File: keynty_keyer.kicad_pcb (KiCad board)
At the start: 2 copper layers, 60 x 35 mm, 32 parts, among them J1 Key Input, J2 Conn_01x03, J3 Conn_01x03, J4 Keyed Output, Q1 BS170, SW1 Power, SW2 IAMBIC Mode, SW3 Sidetone Enable, U1 4081, U2 4071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

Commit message: changed output jack connections, corrected mosfet
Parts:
- J4: value Keyed Output -> Key Input
- Q1: value BS170 -> ZXM61N02FTC; footprint Package_TO_SOT_SMD:SOT-23-3 -> Package_TO_SOT_SMD:SOT-23
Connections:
- J4 pad R: (no net) -> Net-(J4-PadR)
- J4 pad S: Net-(J4-PadS) -> Net-(J4-PadR)
- Q1 pad 1: Net-(BZ1--) -> /OUT
- Q1 pad 2: /OUT -> GND
- Q1 pad 3: GND -> Net-(BZ1--)
- RV1 pad MP: GND -> (no net)
- U5 pad 3: Net-(J4-PadS) -> Net-(J4-PadR)
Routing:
- net Net-(J4-PadR): track 0.00 -> 52.2 mm, vias 0 -> 1
- net Net-(J4-PadS): track 41.9 -> 0.00 mm, vias 1 -> 0
- net Net-(BZ1--): track 28.9 -> 28.1 mm
- net GND: vias 14 -> 15

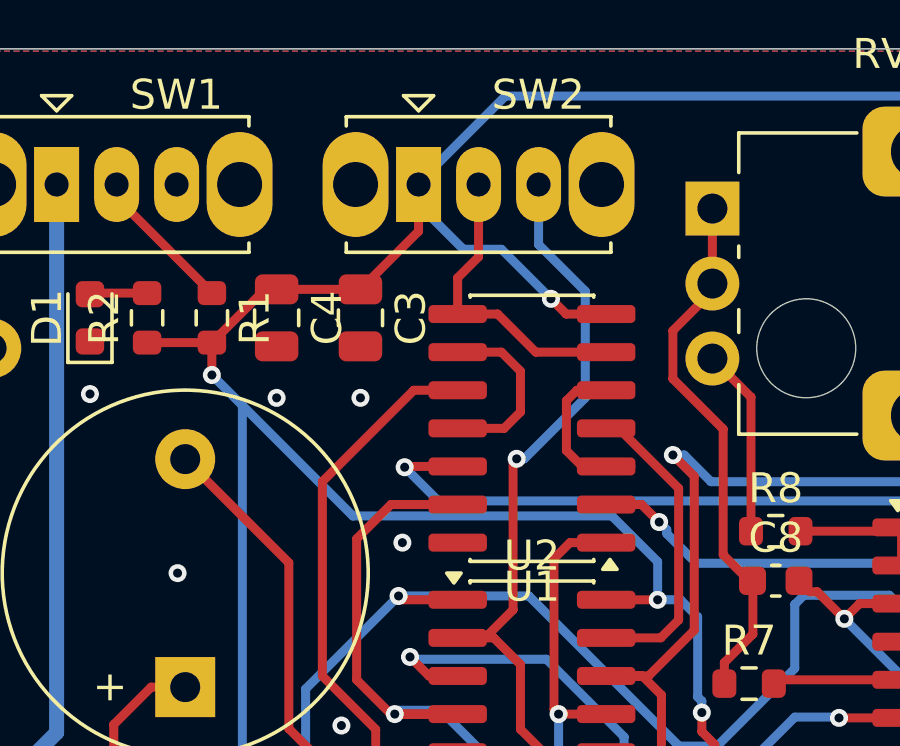
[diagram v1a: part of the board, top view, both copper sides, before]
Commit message: correct powwer supply inverted
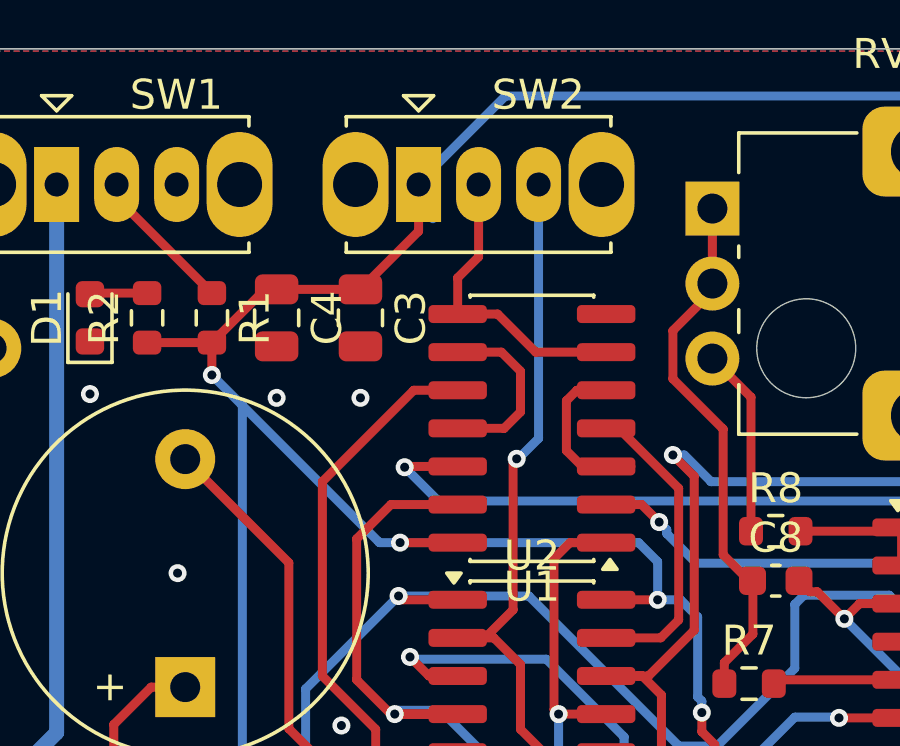
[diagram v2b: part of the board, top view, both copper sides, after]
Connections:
- U1 pad 14: GND -> VCC
- U1 pad 7: VCC -> GND
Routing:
- net VCC: track 170.1 -> 165.0 mm
- net /DASH+DOT: track 26.0 -> 24.6 mm
- net GND: vias 15 -> 14

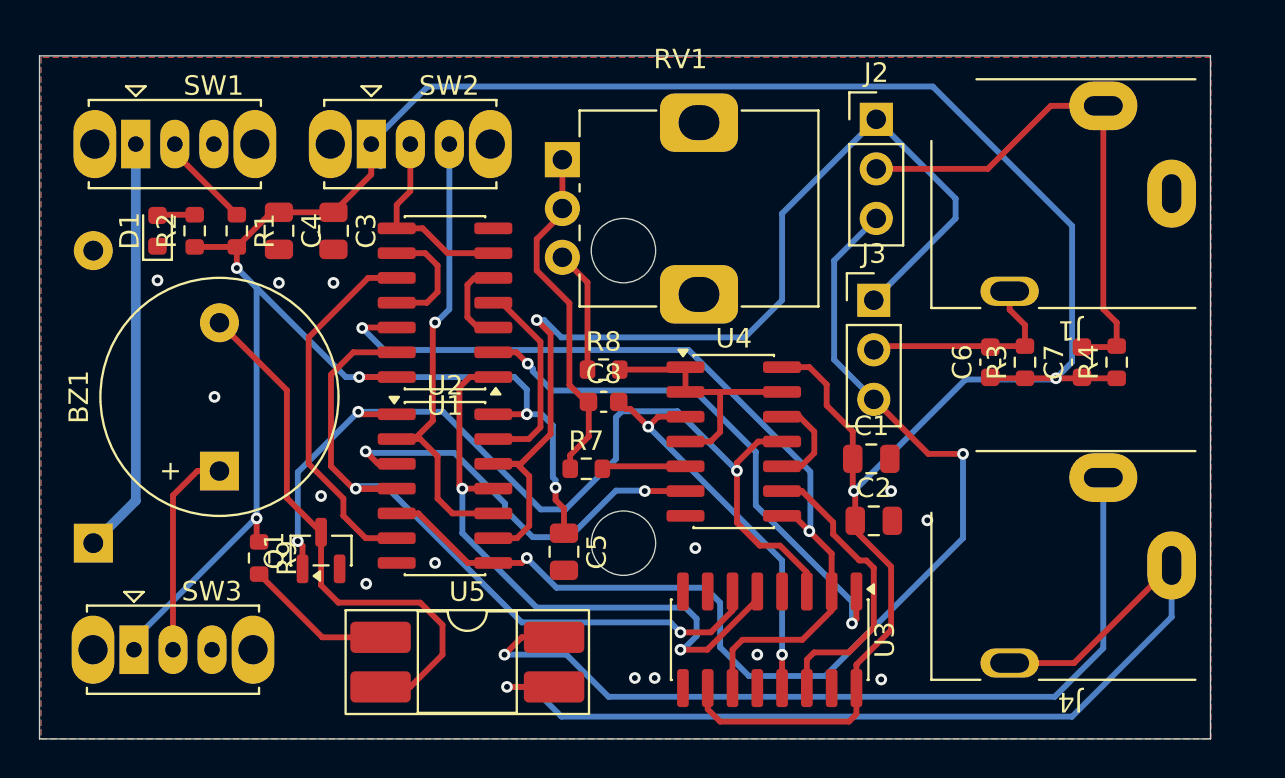
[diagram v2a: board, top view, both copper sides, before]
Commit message: changed pull down ok the inputs
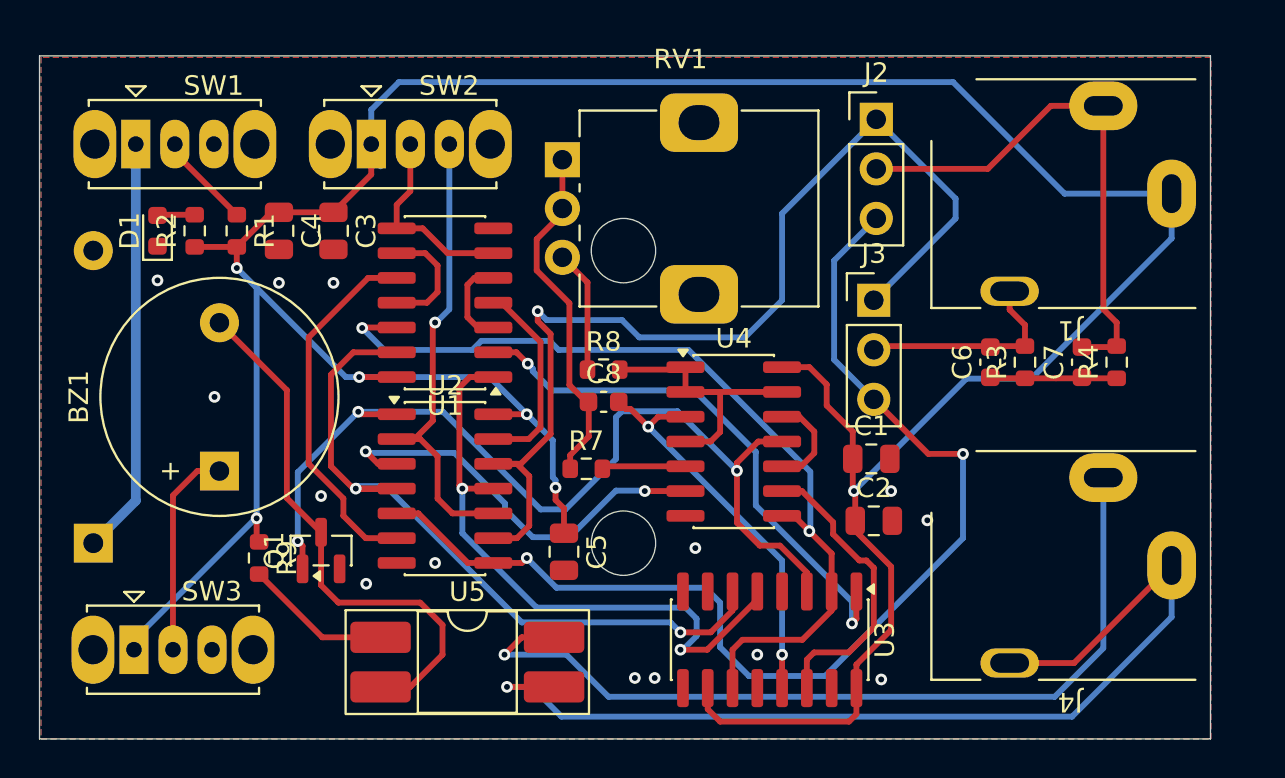
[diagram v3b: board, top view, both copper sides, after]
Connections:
- C6 pad 1: VCC -> GND
- C7 pad 1: VCC -> GND
- J1 pad S: GND -> VCC
- R3 pad 1: VCC -> GND
- R4 pad 1: VCC -> GND
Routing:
- net GND: track 0.00 -> 6.50 mm
- net VCC: track 165.0 -> 165.9 mm, vias 7 -> 6
- net /DASH: track 53.1 -> 53.7 mm

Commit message: refdes position adjusted and clean-up back silkscreen
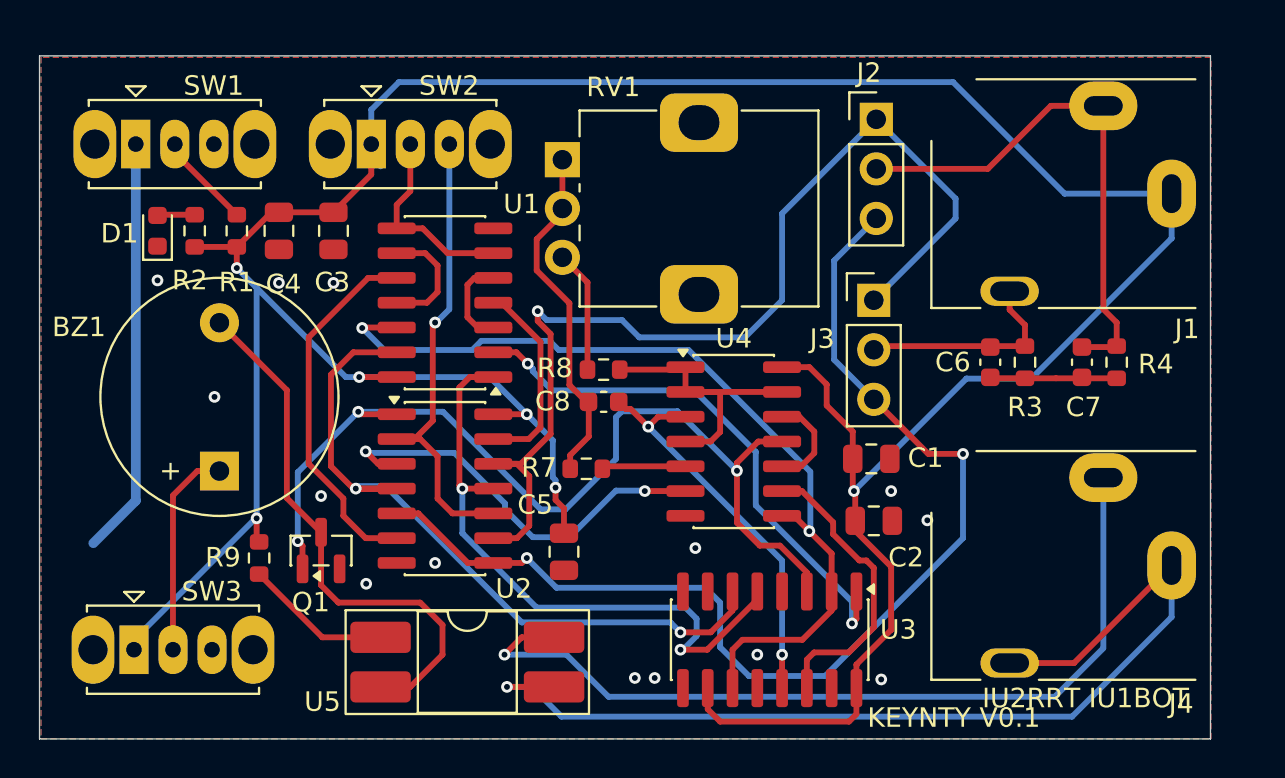
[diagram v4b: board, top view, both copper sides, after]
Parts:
- removed BT1: 3.7V Lithium, Battery:BatteryHolder_Keystone_2462_2xAA
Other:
- board text added: "IU2RRT IU1BOT"
- board text added: "KEYNTY V0.1"

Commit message: corrected battery footprint, added QR, changed minor silkscreen
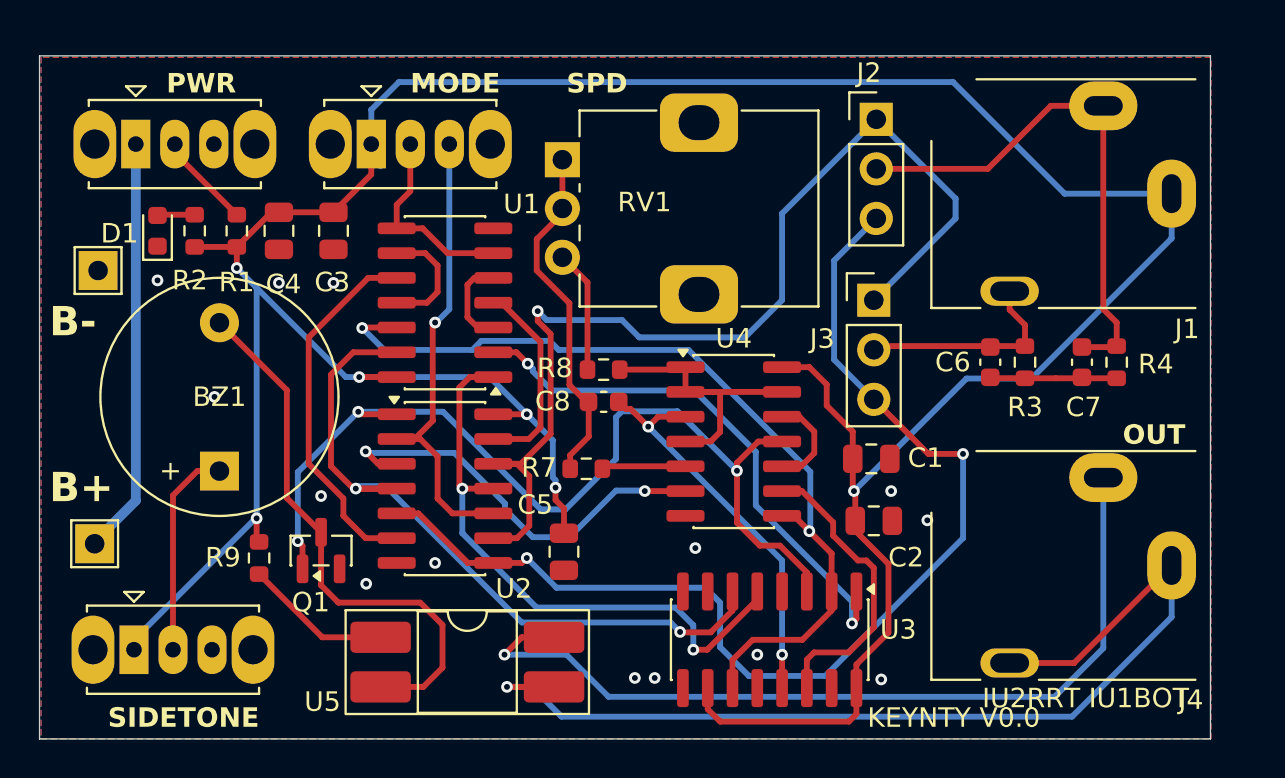
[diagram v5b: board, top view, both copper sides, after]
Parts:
- added J5: Conn_01x01, TestPoint:TestPoint_THTPad_2.0x2.0mm_Drill1.0mm, F.Cu at (102.8, 125.0)
- added J6: Conn_01x01, TestPoint:TestPoint_THTPad_2.0x2.0mm_Drill1.0mm, F.Cu at (103.0, 111.0)
- R3, R4: value R -> 10k
- R9: value R -> 470
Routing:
- net Net-(U3A-K): track 32.3 -> 30.9 mm
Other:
- board text added: "B+"
- board text added: "B-"
- board text added: "KEYNTY V0.0"
- board text added: "MAT___ ___ONI"
- board text added: "MODE"
- board text added: "OUT"
- board text added: "PWR"
- board text added: "SIDETONE"
- board text added: "SPD"
- board text added: "XZGROUP"
- board text removed: "KEYNTY V0.1"
